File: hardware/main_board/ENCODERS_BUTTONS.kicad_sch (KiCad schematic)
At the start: 5 parts, among them J6 Conn_01x05_Pin, J7 Conn_01x05_Pin, J8 2x5 Socket Pins

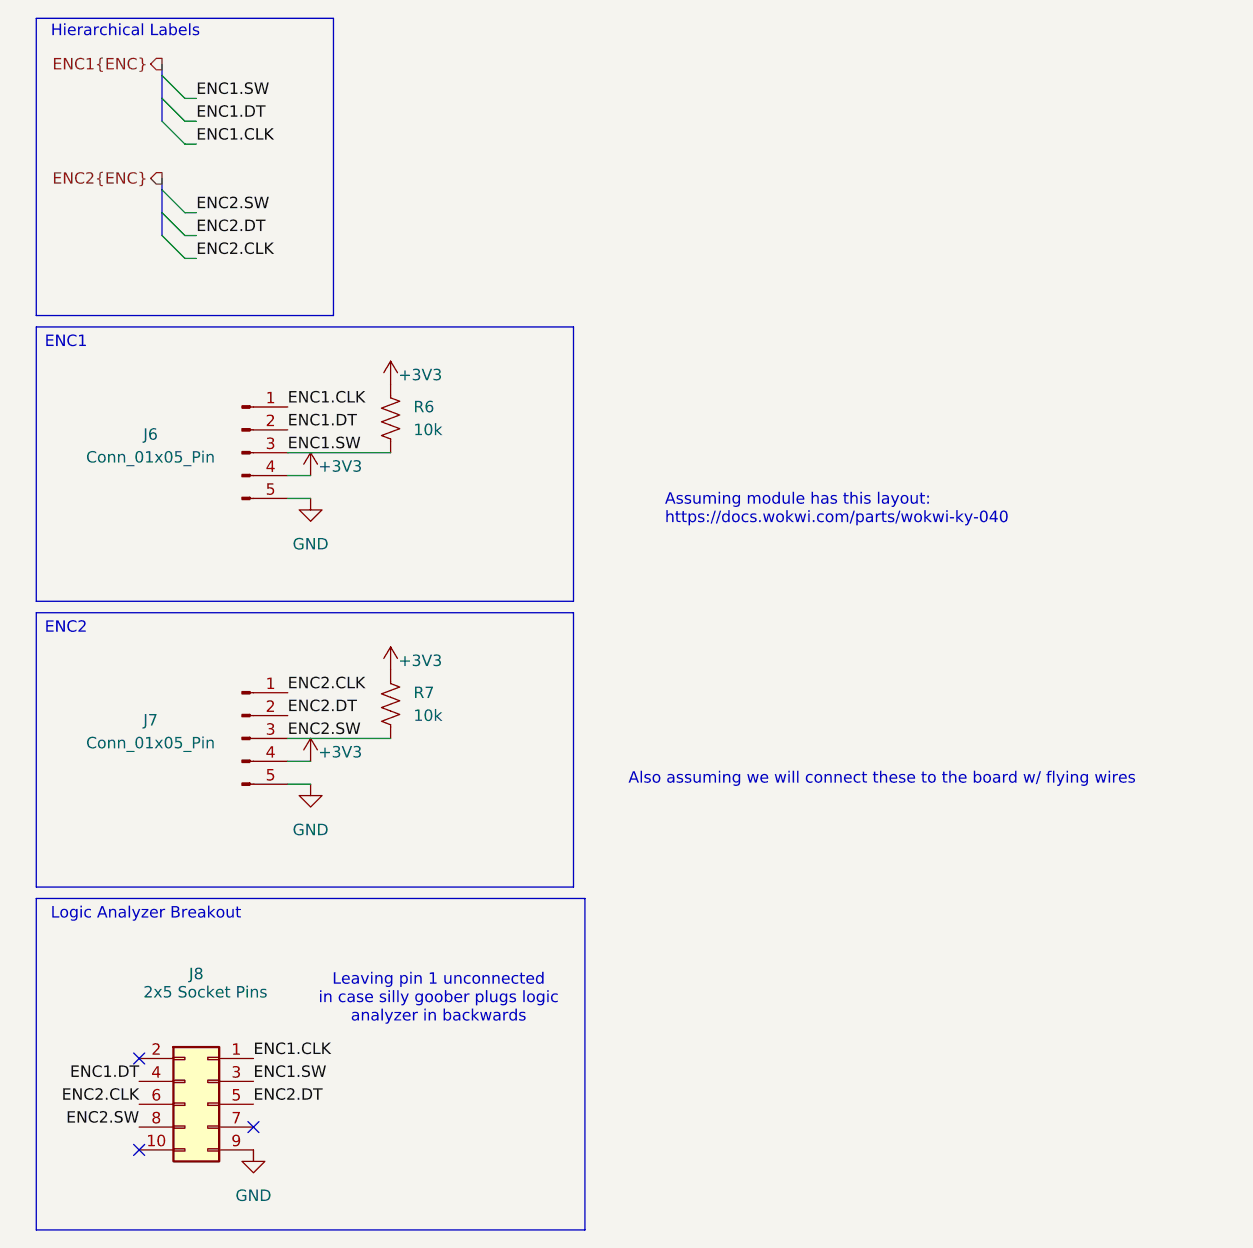
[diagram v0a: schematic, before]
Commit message: main board stuff. removed usbc for power. added level shifter for led logic signal. added lights for mux select signals. finished layout + pass DRC
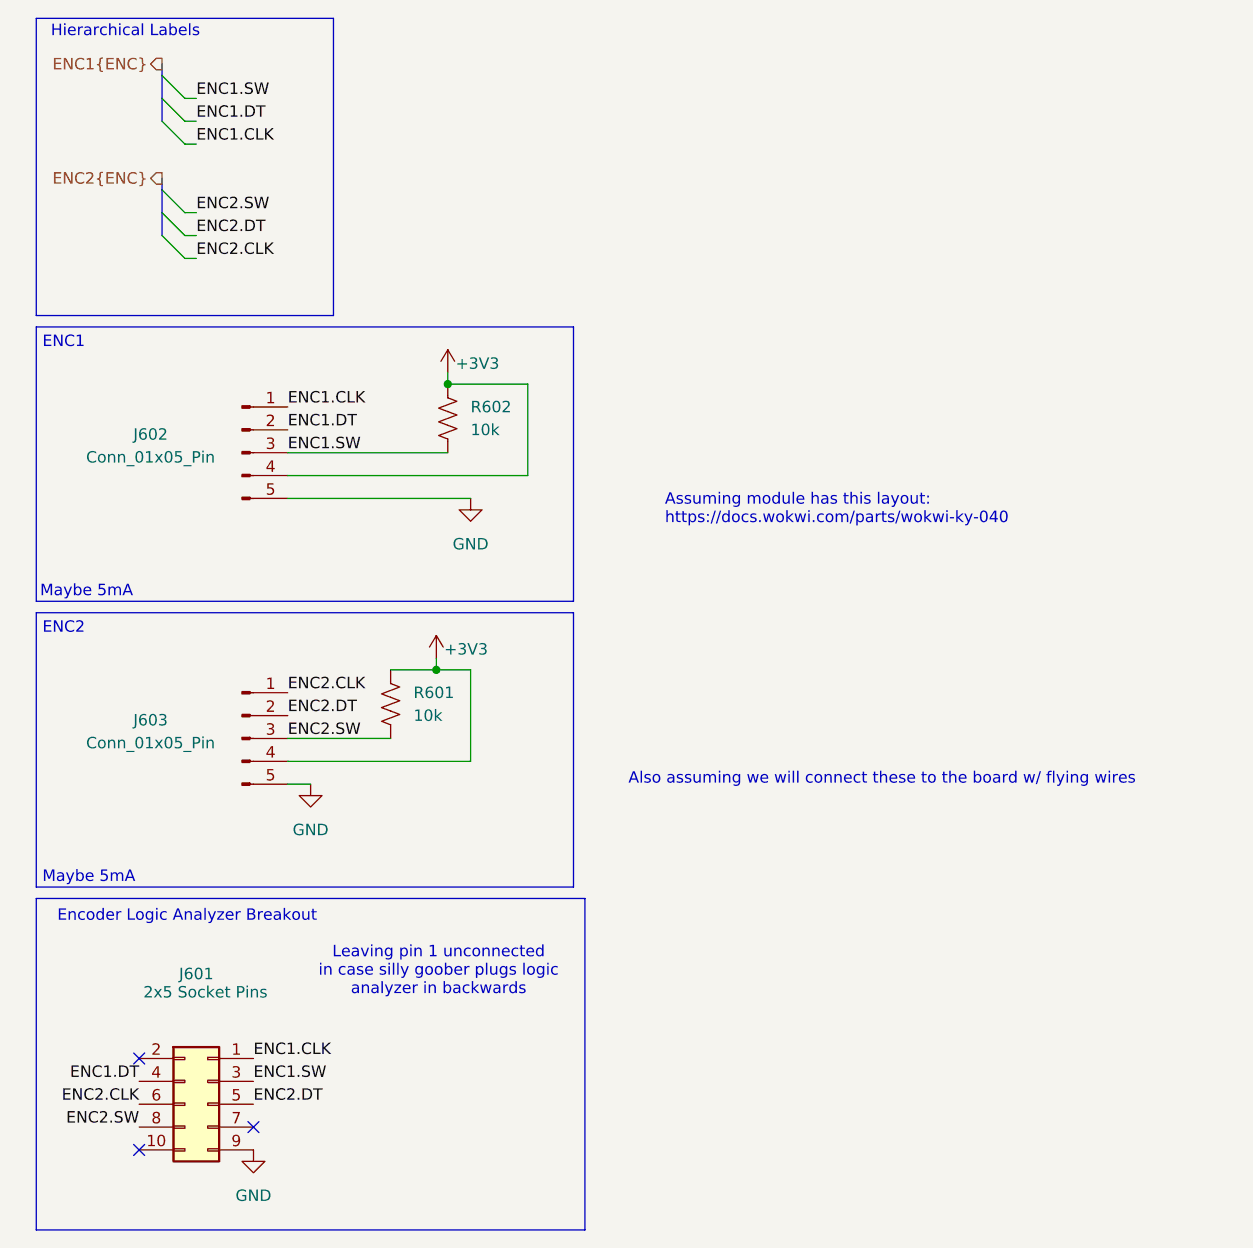
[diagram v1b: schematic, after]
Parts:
- renumbered J8 to J601, J6 to J602, J7 to J603, R7 to R601, R6 to R602
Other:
- note added: "Encoder Logic Analyzer Breakout"
- note added: "Maybe 5mA"
- note removed: "Logic Analyzer Breakout"
- moved on the sheet: R602

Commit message: bom
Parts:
- J601, J602, J603: now left out of the parts list
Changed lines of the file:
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@@
 		(unit 1)
 		(exclude_from_sim no)
-		(in_bom yes)
+		(in_bom no)
 		(on_board yes)
 		(dnp no)
@@
 		(unit 1)
 		(exclude_from_sim no)
-		(in_bom yes)
+		(in_bom no)
 		(on_board yes)
 		(dnp no)
@@
 		(unit 1)
 		(exclude_from_sim no)
-		(in_bom yes)
-		(on_board yes)
-		(dnp no)
+		(in_bom no)
+		(on_board yes)
+		(dnp no)

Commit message: led info
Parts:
- R601, R602: Mouser Price/Stock (none) -> https://www.mouser.com/ProductDetail/YAGEO/RV0805JR-0710KL?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
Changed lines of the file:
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@@
+			)
+		)
+		(property "Mouser Price/Stock" "https://www.mouser.com/ProductDetail/YAGEO/RV0805JR-0710KL?qs=qpJ%252B%252B%252Bdg6p3bGiIDT3p%252B0w%3D%3D"
+			(at 58.42 58.42 0)
+			(effects
+				(font
+					(size 1.27 1.27)
+				)
+				(hide yes)
 			)
 		)
@@
 			(at 52.07 90.17 0)
 			(effects
+				(font
+					(size 1.27 1.27)
+				)
+				(hide yes)
+			)
+		)
+		(property "Mouser Price/Stock" "https://www.mouser.com/ProductDetail/YAGEO/RV0805JR-0710KL?qs=qpJ%252B%252B%252Bdg6p3bGiIDT3p%252B0w%3D%3D"
+			(at 52.07 90.17 0)
+			(effects
